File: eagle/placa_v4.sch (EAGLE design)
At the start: 20 parts, among them IC1 7805

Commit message: Circuito
git-svn-id: https://mbs-bot.googlecode.com/svn/trunk@202 3c29fe3e-da84-11de-ae71-c59d11f48c9c
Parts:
- added R4: 10k, SparkFun:RESISTORPTH-1/2W
- added R5: 4k7, SparkFun:RESISTORPTH-1/2W
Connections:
- new net N$11: DRIVER.SIG1A, MCU.PD7(AIN1/PCINT23)
- new net N$12: DRIVER.SIG1B, MCU.PB0(ICP1/CLKO/PCINT0)
- new net N$13: DRIVER.SIG2B, MCU.PB4(MISO/PCINT4)
- new net N$14: DRIVER.SIG2A, MCU.PB1(OC1A/PCINT1)
- new net N$9: MCU.PC0(ADC0/PCINT8), R4.2, R5.1
- net GND: now also R5.2
- net VCC: now also R4.1
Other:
- moved on the sheet: C1, C2, C9, MCU, R1, R2, R3, Y1

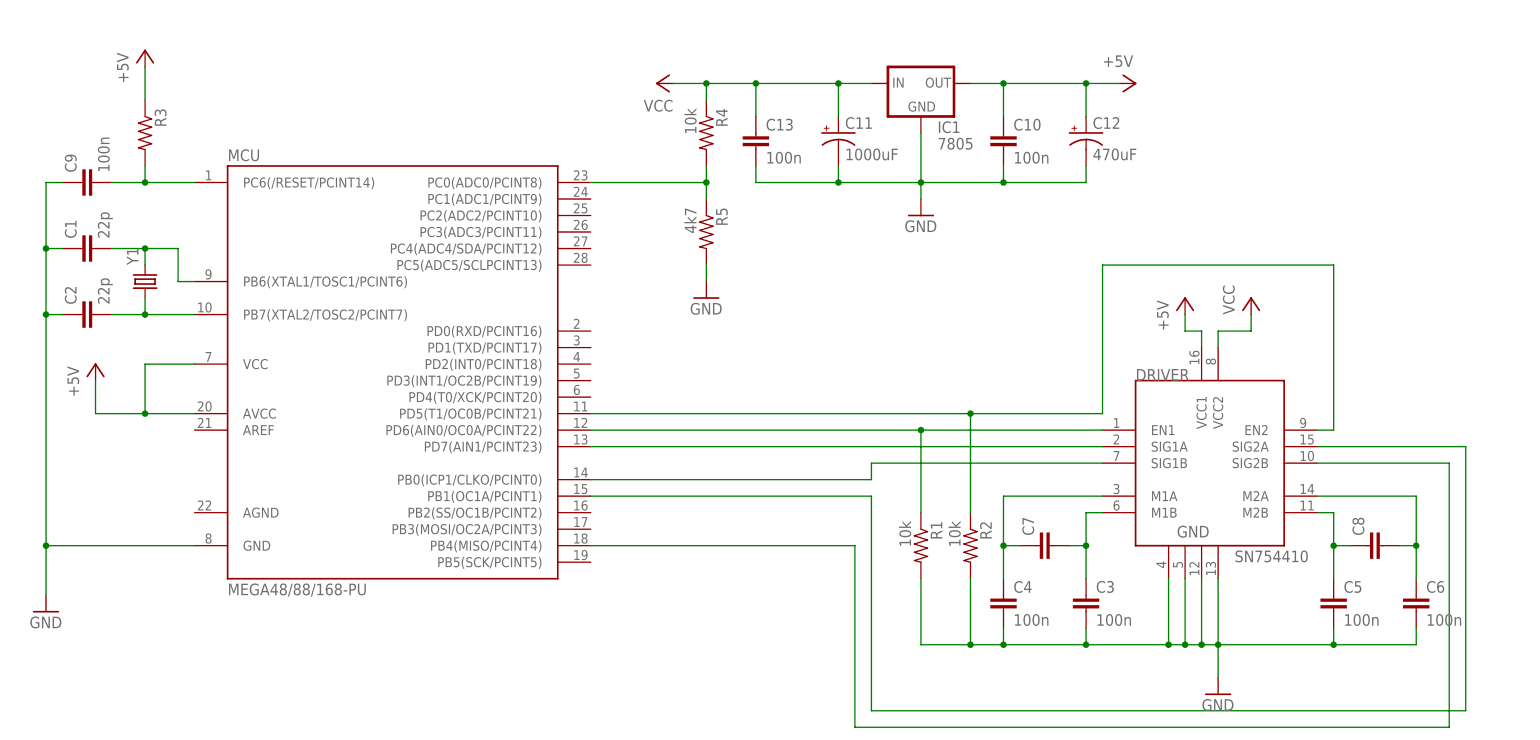
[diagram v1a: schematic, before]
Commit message: Suporte a controlador de motor sem inversor pras pontes H. Removido variaveis deprecated.
git-svn-id: https://mbs-bot.googlecode.com/svn/trunk@203 3c29fe3e-da84-11de-ae71-c59d11f48c9c
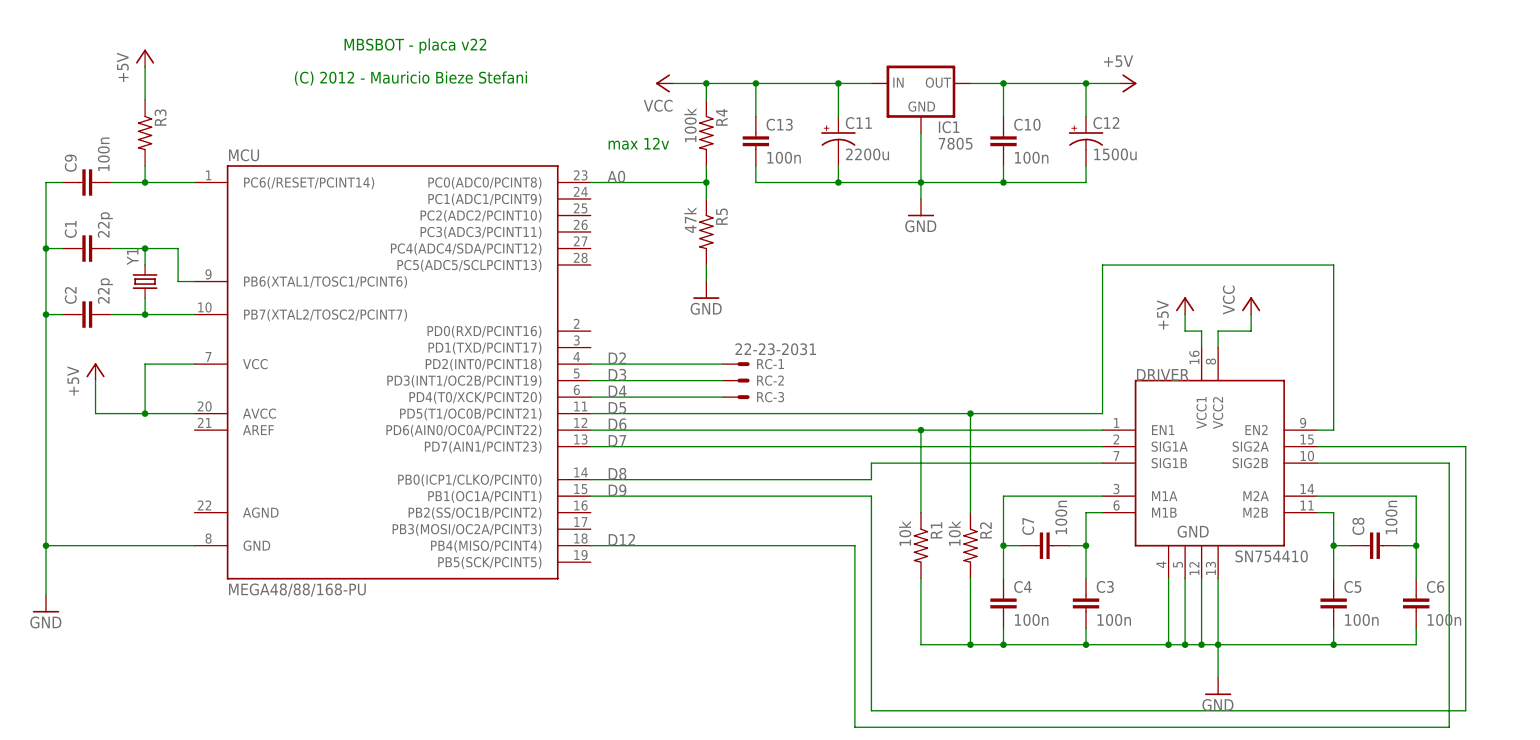
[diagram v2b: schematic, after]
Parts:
- added RC: 22-23-2031, con-molex:22-23-2031
- C11: value 1000uF -> 2200u
- C12: value 470uF -> 1500u
- C7, C8: value (none) -> 100n
- R4: value 10k -> 100k
- R5: value 4k7 -> 47k
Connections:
- net N$1 renamed D6
- net N$11 renamed D7
- net N$12 renamed D8
- net N$13 renamed D12
- net N$14 renamed D9
- net N$2 renamed D5
- net N$9 renamed A0
- new net D2: MCU.PD2(INT0/PCINT18), RC-1.S
- new net D3: MCU.PD3(INT1/OC2B/PCINT19), RC-2.S
- new net D4: MCU.PD4(T0/XCK/PCINT20), RC-3.S
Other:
- note added: "(C) 2012 - Mauricio Bieze Stefani"
- note added: "MBSBOT - placa v22"
- note added: "max 12v"
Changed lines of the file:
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@@
 <setting verticaltext="up"/>
 </settings>
-<grid distance="0.1" unitdist="inch" unit="inch" style="lines" multiple="1" display="no" altdistance="0.01" altunitdist="inch" altunit="inch"/>
+<grid distance="0.1" unitdist="inch" unit="inch" style="lines" multiple="1" display="yes" altdistance="0.01" altunitdist="inch" altunit="inch"/>
 <layers>
 <layer number="1" name="Top" color="4" fill="1" visible="no" active="no"/>
@@
 <part name="C5" library="SparkFun" deviceset="CAP" device="PTH1" value="100n"/>
 <part name="C6" library="SparkFun" deviceset="CAP" device="PTH1" value="100n"/>
-<part name="C7" library="SparkFun" deviceset="CAP" device="PTH1"/>
-<part name="C8" library="SparkFun" deviceset="CAP" device="PTH1"/>
+<part name="C7" library="SparkFun" deviceset="CAP" device="PTH1" value="100n"/>
+<part name="C8" library="SparkFun" deviceset="CAP" device="PTH1" value="100n"/>
 <part name="P+4" library="supply1" deviceset="+5V" device=""/>
 <part name="C9" library="SparkFun" deviceset="CAP" device="PTH1" value="100n"/>
@@
 <part name="GND3" library="supply1" deviceset="GND" device=""/>
 <part name="C10" library="SparkFun" deviceset="CAP" device="PTH1" value="100n"/>
-<part name="C11" library="SparkFun" deviceset="CAP_POL" device="PTH1" value="1000uF"/>
-<part name="C12" library="SparkFun" deviceset="CAP_POL" device="PTH1" value="470uF"/>
+<part name="C11" library="SparkFun" deviceset="CAP_POL" device="PTH1" value="2200u"/>
+<part name="C12" library="SparkFun" deviceset="CAP_POL" device="PTH1" value="1500u"/>
 <part name="C13" library="SparkFun" deviceset="CAP" device="PTH1" value="100n"/>
-<part name="R4" library="SparkFun" deviceset="RESISTOR" device="PTH-1/2W" value="10k"/>
-<part name="R5" library="SparkFun" deviceset="RESISTOR" device="PTH-1/2W" value="4k7"/>
+<part name="R4" library="SparkFun" deviceset="RESISTOR" device="PTH-1/2W" value="100k"/>
+<part name="R5" library="SparkFun" deviceset="RESISTOR" device="PTH-1/2W" value="47k"/>
 <part name="GND4" library="supply1" deviceset="GND" device=""/>
+<part name="RC" library="con-molex" deviceset="22-23-2031" device=""/>
 </parts>
 <sheets>
 <sheet>
 <plain>
+<text x="5.08" y="106.68" size="1.778" layer="91">(C) 2012 - Mauricio Bieze Stefani</text>
+<text x="12.7" y="111.76" size="1.778" layer="91">MBSBOT - placa v22</text>
+<text x="53.34" y="96.52" size="1.778" layer="91">max 12v</text>
 </plain>
 <instances>
@@
 <instance part="R5" gate="G$1" x="68.58" y="83.82" rot="R270"/>
 <instance part="GND4" gate="1" x="68.58" y="73.66"/>
+<instance part="RC" gate="-1" x="73.66" y="63.5"/>
+<instance part="RC" gate="-2" x="73.66" y="60.96"/>
+<instance part="RC" gate="-3" x="73.66" y="58.42"/>
 </instances>
 <busses>
 </busses>
 <nets>
-<net name="N$1" class="0">
+<net name="D6" class="0">
 <segment>
 <pinref part="R1" gate="G$1" pin="1"/>
@@
 <wire x1="50.8" y1="53.34" x2="101.6" y2="53.34" width="0.1524" layer="91"/>
 <junction x="101.6" y="53.34"/>
-</segment>
-</net>
-<net name="N$2" class="0">
+<label x="53.34" y="53.34" size="1.778" layer="95"/>
+</segment>
+</net>
+<net name="D5" class="0">
 <segment>
 <pinref part="DRIVER" gate="G$1" pin="EN2"/>
@@
 <wire x1="109.22" y1="55.88" x2="109.22" y2="40.64" width="0.1524" layer="91"/>
 <junction x="109.22" y="55.88"/>
+<label x="53.34" y="55.88" size="1.778" layer="95"/>
 </segment>
 </net>
@@
 </segment>
 </net>
-<net name="N$11" class="0">
+<net name="D7" class="0">
 <segment>
 <pinref part="MCU" gate="1" pin="PD7(AIN1/PCINT23)"/>
 <pinref part="DRIVER" gate="G$1" pin="SIG1A"/>
 <wire x1="50.8" y1="50.8" x2="129.54" y2="50.8" width="0.1524" layer="91"/>
-</segment>
-</net>
-<net name="N$12" class="0">
+<label x="53.34" y="50.8" size="1.778" layer="95"/>
+</segment>
+</net>
+<net name="D8" class="0">
 <segment>
 <pinref part="MCU" gate="1" pin="PB0(ICP1/CLKO/PCINT0)"/>
@@
 <pinref part="DRIVER" gate="G$1" pin="SIG1B"/>
 <wire x1="93.98" y1="48.26" x2="129.54" y2="48.26" width="0.1524" layer="91"/>
-</segment>
-</net>
-<net name="N$13" class="0">
+<label x="53.34" y="45.72" size="1.778" layer="95"/>
+</segment>
+</net>
+<net name="D12" class="0">
 <segment>
 <pinref part="MCU" gate="1" pin="PB4(MISO/PCINT4)"/>
@@
 <pinref part="DRIVER" gate="G$1" pin="SIG2B"/>
 <wire x1="182.88" y1="48.26" x2="162.56" y2="48.26" width="0.1524" layer="91"/>
-</segment>
-</net>
-<net name="N$14" class="0">
+<label x="53.34" y="35.56" size="1.778" layer="95"/>
+</segment>
+</net>
+<net name="D9" class="0">
 <segment>
 <pinref part="DRIVER" gate="G$1" pin="SIG2A"/>
@@
 <pinref part="MCU" gate="1" pin="PB1(OC1A/PCINT1)"/>
 <wire x1="93.98" y1="43.18" x2="50.8" y2="43.18" width="0.1524" layer="91"/>
-</segment>
-</net>
-<net name="N$9" class="0">
+<label x="53.34" y="43.18" size="1.778" layer="95"/>
+</segment>
+</net>
+<net name="A0" class="0">
 <segment>
 <pinref part="R4" gate="G$1" pin="2"/>
@@
 <wire x1="50.8" y1="91.44" x2="68.58" y2="91.44" width="0.1524" layer="91"/>
 <junction x="68.58" y="91.44"/>
-</segment>
-</net>
+<label x="53.34" y="91.44" size="1.778" layer="95"/>
+</segment>
+</net>
+<net name="D3" class="0">
+<segment>
+<pinref part="MCU" gate="1" pin="PD3(INT1/OC2B/PCINT19)"/>
+<pinref part="RC" gate="-2" pin="S"/>
+<wire x1="50.8" y1="60.96" x2="71.12" y2="60.96" width="0.1524" layer="91"/>
+<label x="53.34" y="60.96" size="1.778" layer="95"/>
+</segment>
+</net>
+<net name="D4" class="0">
+<segment>
+<pinref part="MCU" gate="1" pin="PD4(T0/XCK/PCINT20)"/>
+<pinref part="RC" gate="-3" pin="S"/>
+<wire x1="50.8" y1="58.42" x2="71.12" y2="58.42" width="0.1524" layer="91"/>
+<label x="53.34" y="58.42" size="1.778" layer="95"/>
+</segment>
+</net>
+<net name="D2" class="0">
+<segment>
+<pinref part="MCU" gate="1" pin="PD2(INT0/PCINT18)"/>
+<pinref part="RC" gate="-1" pin="S"/>
+<wire x1="50.8" y1="63.5" x2="71.12" y2="63.5" width="0.1524" layer="91"/>
+<label x="53.34" y="63.5" size="1.778" layer="95"/>
+</segment>
+</net>

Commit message: Eletronica do Winchester
git-svn-id: https://mbs-bot.googlecode.com/svn/trunk@205 3c29fe3e-da84-11de-ae71-c59d11f48c9c
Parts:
- added JP1: AVR-ISP-6VERT, avr-7:AVR-ISP-6VERT
- R3: value (none) -> 10k
- RC: value 22-23-2031 -> (none); device con-molex:22-23-2031 -> con-lstb:MA03-1
- Y1: value (none) -> 16MHz
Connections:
- new net N$2: JP1.3, MCU.PB5(SCK/PCINT5)
- new net N$9: JP1.4, MCU.PB3(MOSI/OC2A/PCINT3)
- net +5V: now also JP1.2
- net D12: now also JP1.1
- net D2: now also RC.1; no longer RC-1.S
- net D3: now also RC.2; no longer RC-2.S
- net D4: now also RC.3; no longer RC-3.S
- net GND: now also JP1.6, MCU.AGND
- net N$10: now also C9.2, JP1.5
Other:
- moved on the sheet: C10, C11, C12, C13, IC1, R3, R4, R5

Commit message: Bugfix e hardware da arma
git-svn-id: https://mbs-bot.googlecode.com/svn/trunk@209 3c29fe3e-da84-11de-ae71-c59d11f48c9c
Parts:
- added A: (no value), con-lstb:MA05-1
- added ARMA: (no value), con-wago-500:W237-102
- added BT: (no value), con-lstb:MA04-1
- added LED1: (no value), SparkFun:LED3MM
- added Q1: IRF740, transistor-power:IRF740
- added R6, R7: 1k, SparkFun:RESISTORKIT
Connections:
- net N$9 renamed D11
- new net A: BT.1, MCU.PD0(RXD/PCINT16)
- new net D13: JP1.3, LED1.A, MCU.PB5(SCK/PCINT5)
- new net N$1: LED1.C, R6.2
- new net N$11: ARMA-2.KL, Q1.D
- new net N$12: A.1, MCU.PC1(ADC1/PCINT9)
- new net N$13: A.2, MCU.PC2(ADC2/PCINT10)
- new net N$14: A.3, MCU.PC3(ADC3/PCINT11)
- new net N$15: A.4, MCU.PC4(ADC4/SDA/PCINT12)
- new net N$16: A.5, MCU.PC5(ADC5/SCLPCINT13)
- new net N$9: BT.2, MCU.PD1(TXD/PCINT17)
- net D9: now also MCU.PB2(SS/OC1B/PCINT2), R7.1
- net GND: now also Q1.S, R6.1
- net N$2: now also Q1.G, R7.2; no longer JP1.3, MCU.PB5(SCK/PCINT5)
- net VCC: now also ARMA-1.KL

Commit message: Eletronica
git-svn-id: https://mbs-bot.googlecode.com/svn/trunk@210 3c29fe3e-da84-11de-ae71-c59d11f48c9c
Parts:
- added MOTOR_DIR, MOTOR_ESQ: (no value), con-wago-500:W237-102
- BT: device con-lstb:MA04-1 -> con-lstb:MA05-1
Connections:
- net A: now also BT.4; no longer BT.1
- net N$5: now also MOTOR_ESQ-2.KL
- net N$6: now also MOTOR_ESQ-1.KL
- net N$7: now also MOTOR_DIR-1.KL
- net N$8: now also MOTOR_DIR-2.KL
- net N$9: now also BT.5; no longer BT.2
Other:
- moved on the sheet: A, C7, C8, Q1
